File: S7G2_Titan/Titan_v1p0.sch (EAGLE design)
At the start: 87 parts, among them J1 4-pos, J10 40-pos, J11 10-pos, J12 10-pos, J2 USB-B-Micro, J3 USB-A, J6 10-pos, J9 SD_CARD_1140084168, U2 AP2151DWG-7, U3 KSZ8081RNACAQFN-24-M, U4 S7G2LQFP176, X3 32.768KHz, X4 24MHz

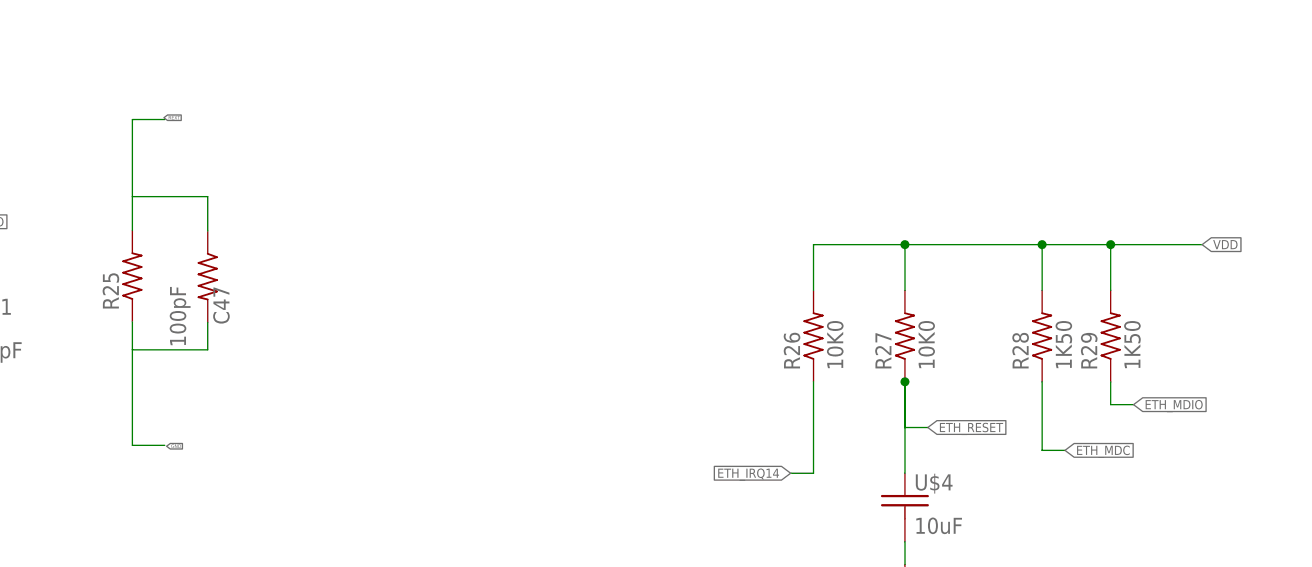
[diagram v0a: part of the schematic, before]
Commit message: Updated Parts
Updated parts with manufacturer part numbers.
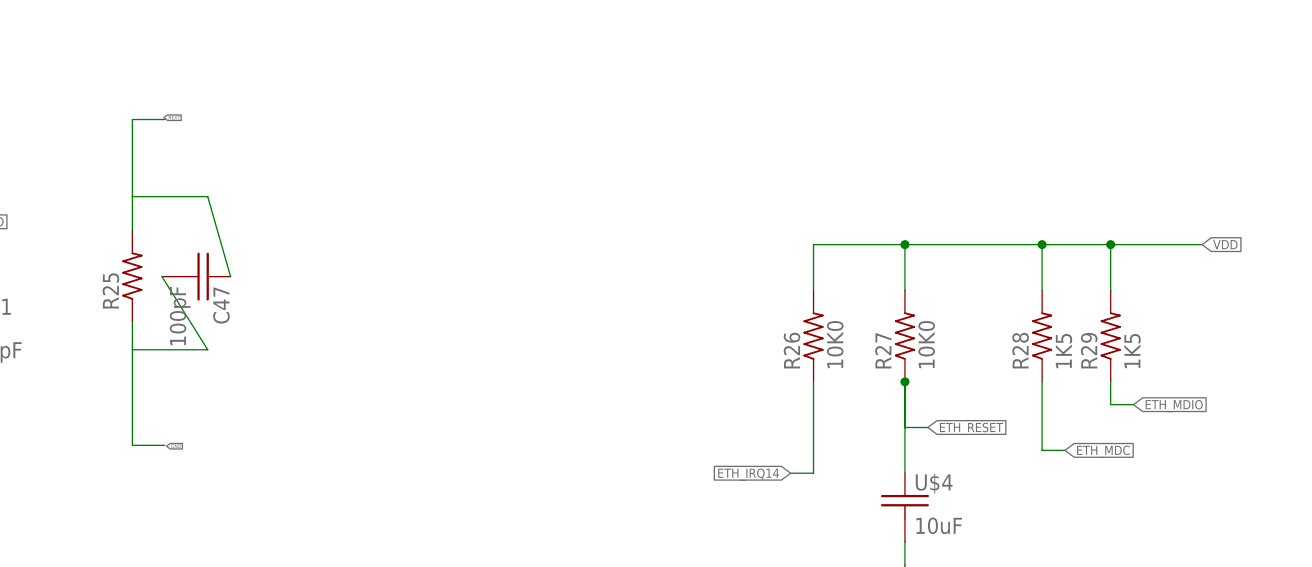
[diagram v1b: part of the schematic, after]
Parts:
- C41, C42: device 3D_MIG_Controller:C_0402 -> 3D_MIG_Controller:C_0402_24PF
- C44, C46, C49, C61: device 3D_MIG_Controller:C_0402 -> 3D_MIG_Controller:C_0402_0.1UF
- C45: device 3D_MIG_Controller:C_0402 -> 3D_MIG_Controller:C_0402_2.2UF
- C47: device 3D_MIG_Controller:R_0402 -> 3D_MIG_Controller:C_0402_100PF
- R25: value 6k49 -> 6K49; device 3D_MIG_Controller:R_0402 -> 3D_MIG_Controller:R_0402_6K49
- R28, R29: value 1K50 -> 1K5; device 3D_MIG_Controller:R_0402 -> 3D_MIG_Controller:R_0402_1K5
- R30, R31, R32, R33: device 3D_MIG_Controller:R_0402 -> 3D_MIG_Controller:R_0402_33R0
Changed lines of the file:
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@@
 <layer number="115" name="ReferenceISLANDS" color="7" fill="1" visible="yes" active="yes"/>
 <layer number="116" name="Patch_BOT" color="9" fill="4" visible="yes" active="yes"/>
+<layer number="117" name="PM_Ref" color="7" fill="1" visible="yes" active="yes"/>
 <layer number="118" name="Rect_Pads" color="7" fill="1" visible="yes" active="yes"/>
+<layer number="119" name="PF_Ref" color="7" fill="1" visible="yes" active="yes"/>
+<layer number="120" name="WFL_Ref" color="7" fill="1" visible="yes" active="yes"/>
 <layer number="121" name="_tsilk" color="7" fill="1" visible="yes" active="yes"/>
 <layer number="122" name="_bsilk" color="7" fill="1" visible="yes" active="yes"/>
@@
 <part name="C40" library="3D_MIG_Controller" deviceset="C_0402_0.1UF" device="" value="0.1uF"/>
 <part name="U$3" library="3D_MIG_Controller" deviceset="XTAL_25_MHZ" device="" value="25MHz"/>
-<part name="C41" library="3D_MIG_Controller" deviceset="C_0402" device="" value="24pF"/>
-<part name="C42" library="3D_MIG_Controller" deviceset="C_0402" device="" value="24pF"/>
-<part name="R25" library="3D_MIG_Controller" deviceset="R_0402" device="" value="6k49"/>
+<part name="C41" library="3D_MIG_Controller" deviceset="C_0402_24PF" device="" value="24pF"/>
+<part name="C42" library="3D_MIG_Controller" deviceset="C_0402_24PF" device="" value="24pF"/>
+<part name="R25" library="3D_MIG_Controller" deviceset="R_0402_6K49" device="" value="6K49"/>
 <part name="C43" library="3D_MIG_Controller" deviceset="C_0402_22UF" device="" value="22uF"/>
-<part name="C44" library="3D_MIG_Controller" deviceset="C_0402" device="" value="0.1uF"/>
-<part name="C45" library="3D_MIG_Controller" deviceset="C_0402" device="" value="2.2uF"/>
-<part name="C46" library="3D_MIG_Controller" deviceset="C_0402" device="" value="0.1uF"/>
+<part name="C44" library="3D_MIG_Controller" deviceset="C_0402_0.1UF" device="" value="0.1uF"/>
+<part name="C45" library="3D_MIG_Controller" deviceset="C_0402_2.2UF" device="" value="2.2uF"/>
+<part name="C46" library="3D_MIG_Controller" deviceset="C_0402_0.1UF" device="" value="0.1uF"/>
 <part name="FB2/2" library="3D_MIG_Controller" deviceset="FB_0603_120_OHM" device="0603" value="120Ohm"/>
 <part name="R26" library="3D_MIG_Controller" deviceset="R_0402_10K0" device="" value="10K0"/>
 <part name="R27" library="3D_MIG_Controller" deviceset="R_0402_10K0" device="" value="10K0"/>
-<part name="R28" library="3D_MIG_Controller" deviceset="R_0402" device="" value="1K50"/>
-<part name="R29" library="3D_MIG_Controller" deviceset="R_0402" device="" value="1K50"/>
-<part name="C47" library="3D_MIG_Controller" deviceset="R_0402" device="" value="100pF"/>
+<part name="R28" library="3D_MIG_Controller" deviceset="R_0402_1K5" device="" value="1K5"/>
+<part name="R29" library="3D_MIG_Controller" deviceset="R_0402_1K5" device="" value="1K5"/>
+<part name="C47" library="3D_MIG_Controller" deviceset="C_0402_100PF" device="" value="100pF"/>
 <part name="GND50" library="3D_MIG_Controller" deviceset="GND" device=""/>
 <part name="GND51" library="3D_MIG_Controller" deviceset="GND" device=""/>
@@
 <part name="GND53" library="3D_MIG_Controller" deviceset="GND" device=""/>
 <part name="C48" library="3D_MIG_Controller" deviceset="C_0402_22UF" device="" value="22uF"/>
-<part name="C49" library="3D_MIG_Controller" deviceset="C_0402" device="" value="0.1uF"/>
+<part name="C49" library="3D_MIG_Controller" deviceset="C_0402_0.1UF" device="" value="0.1uF"/>
 <part name="GND54" library="3D_MIG_Controller" deviceset="GND" device=""/>
 <part name="U$4" library="3D_MIG_Controller" deviceset="C_0402_10UF" device="" value="10uF"/>
@@
 <part name="GND57" library="3D_MIG_Controller" deviceset="GND" device=""/>
 <part name="GND58" library="3D_MIG_Controller" deviceset="GND" device=""/>
-<part name="R30" library="3D_MIG_Controller" deviceset="R_0402" device="" value="33R0"/>
-<part name="R31" library="3D_MIG_Controller" deviceset="R_0402" device="" value="33R0"/>
-<part name="R32" library="3D_MIG_Controller" deviceset="R_0402" device="" value="33R0"/>
-<part name="R33" library="3D_MIG_Controller" deviceset="R_0402" device="" value="33R0"/>
+<part name="R30" library="3D_MIG_Controller" deviceset="R_0402_33R0" device="" value="33R0"/>
+<part name="R31" library="3D_MIG_Controller" deviceset="R_0402_33R0" device="" value="33R0"/>
+<part name="R32" library="3D_MIG_Controller" deviceset="R_0402_33R0" device="" value="33R0"/>
+<part name="R33" library="3D_MIG_Controller" deviceset="R_0402_33R0" device="" value="33R0"/>
 <part name="R1" library="3D_MIG_Controller" deviceset="R_0402_10K0" device="" value="10K0"/>
 <part name="U2" library="3D_MIG_Controller" deviceset="AP2151DWG-7" device=""/>
@@
 <part name="C60" library="3D_MIG_Controller" deviceset="C_0402_0.1UF" device="" value="0.1uF"/>
 <part name="GND77" library="3D_MIG_Controller" deviceset="GND" device=""/>
-<part name="C61" library="3D_MIG_Controller" deviceset="C_0402" device="" value="0.1uF"/>
+<part name="C61" library="3D_MIG_Controller" deviceset="C_0402_0.1UF" device="" value="0.1uF"/>
 <part name="GND78" library="3D_MIG_Controller" deviceset="GND" device=""/>
 <part name="GND79" library="3D_MIG_Controller" deviceset="GND" device=""/>
@@
 <segment>
 <pinref part="C47" gate="G$1" pin="2"/>
-<wire x1="-575.31" y1="-168.656" x2="-575.31" y2="-171.704" width="0.1524" layer="91"/>
+<wire x1="-580.39" y1="-163.576" x2="-575.31" y2="-171.704" width="0.1524" layer="91"/>
 <wire x1="-575.31" y1="-171.704" x2="-583.692" y2="-171.704" width="0.1524" layer="91"/>
 </segment>
@@
 <segment>
 <pinref part="C47" gate="G$1" pin="1"/>
-<wire x1="-575.31" y1="-158.496" x2="-575.31" y2="-154.686" width="0.1524" layer="91"/>
+<wire x1="-572.77" y1="-163.576" x2="-575.31" y2="-154.686" width="0.1524" layer="91"/>
 <wire x1="-575.31" y1="-154.686" x2="-583.692" y2="-154.686" width="0.1524" layer="91"/>
 </segment>

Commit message: Updated Parts Numbers
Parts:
- J4: value (none) -> RJ45
- J5, J7: value (none) -> 20-pos
- renumbered U$3 to U5
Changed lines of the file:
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@@
 <part name="R13" library="3D_MIG_Controller" deviceset="R_0402_470R0" device="" value="470R0"/>
 <part name="L3" library="3D_MIG_Controller" deviceset="INDUCTOR_1008_2.2_MH_1.3A" device="" value="2.2uH,1.3A,1MOhm"/>
-<part name="J4" library="3D_MIG_Controller" deviceset="RJ45_WITH_ELEC" device=""/>
+<part name="J4" library="3D_MIG_Controller" deviceset="RJ45_WITH_ELEC" device="" value="RJ45"/>
 <part name="U3" library="3D_MIG_Controller" deviceset="KSZ8081RNACA" device="QFN-24-M"/>
 <part name="R23" library="3D_MIG_Controller" deviceset="R_0402_470R0" device="" value="470R0"/>
@@
 <part name="C39" library="3D_MIG_Controller" deviceset="C_0402_0.1UF" device="" value="0.1uF"/>
 <part name="C40" library="3D_MIG_Controller" deviceset="C_0402_0.1UF" device="" value="0.1uF"/>
-<part name="U$3" library="3D_MIG_Controller" deviceset="XTAL_25_MHZ" device="" value="25MHz"/>
+<part name="U5" library="3D_MIG_Controller" deviceset="XTAL_25_MHZ" device="" value="25MHz"/>
 <part name="C41" library="3D_MIG_Controller" deviceset="C_0402_24PF" device="" value="24pF"/>
 <part name="C42" library="3D_MIG_Controller" deviceset="C_0402_24PF" device="" value="24pF"/>
@@
 <part name="C2" library="3D_MIG_Controller" deviceset="C_0402_1UF" device="" value="1uF"/>
 <part name="J1" library="3D_MIG_Controller" deviceset="3.81MM_1_X_4_RT_ANGLE_PLUG_HEADER" device="" value="4-pos"/>
-<part name="J5" library="3D_MIG_Controller" deviceset="2_X_10_HEADER_GENERIC" device=""/>
+<part name="J5" library="3D_MIG_Controller" deviceset="2_X_10_HEADER_GENERIC" device="" value="20-pos"/>
 <part name="J12" library="3D_MIG_Controller" deviceset="CONN_05X2_RA" device="PTH" value="10-pos"/>
-<part name="J7" library="3D_MIG_Controller" deviceset="2_X_10_HEADER_GENERIC" device=""/>
+<part name="J7" library="3D_MIG_Controller" deviceset="2_X_10_HEADER_GENERIC" device="" value="20-pos"/>
 <part name="J6" library="3D_MIG_Controller" deviceset="CONN_05X2_RA" device="PTH" value="10-pos"/>
 </parts>
@@
 <attribute name="VALUE" x="-405.704" y="-208.131" size="1.778" layer="96"/>
 </instance>
-<instance part="U$3" gate="G$1" x="-629.48" y="-159.7" smashed="yes"/>
+<instance part="U5" gate="G$1" x="-629.48" y="-159.7" smashed="yes"/>
 <instance part="C41" gate="G$1" x="-602.32" y="-168.45" smashed="yes">
 <attribute name="NAME" x="-601.304" y="-167.815" size="1.778" layer="95"/>
@@
 </segment>
 <segment>
-<pinref part="U$3" gate="G$1" pin="4"/>
+<pinref part="U5" gate="G$1" pin="4"/>
 <pinref part="GND52" gate="1" pin="GND"/>
 <wire x1="-642.18" y1="-157.16" x2="-665.76" y2="-157.16" width="0.1524" layer="91"/>
@@
 </segment>
 <segment>
-<pinref part="U$3" gate="G$1" pin="2"/>
+<pinref part="U5" gate="G$1" pin="2"/>
 <pinref part="GND53" gate="1" pin="GND"/>
 <wire x1="-616.78" y1="-162.24" x2="-611.4" y2="-162.24" width="0.1524" layer="91"/>
@@
 </segment>
 <segment>
-<pinref part="U$3" gate="G$1" pin="1"/>
+<pinref part="U5" gate="G$1" pin="1"/>
 <pinref part="C42" gate="G$1" pin="1"/>
 <wire x1="-642.18" y1="-162.24" x2="-650.47" y2="-162.24" width="0.1524" layer="91"/>
@@
 </segment>
 <segment>
-<pinref part="U$3" gate="G$1" pin="3"/>
+<pinref part="U5" gate="G$1" pin="3"/>
 <pinref part="C41" gate="G$1" pin="1"/>
 <wire x1="-616.78" y1="-157.16" x2="-602.32" y2="-157.16" width="0.1524" layer="91"/>
